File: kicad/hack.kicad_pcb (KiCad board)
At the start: 2 copper layers, 29.2 x 21.6 mm, 35 parts, among them P1 USB_micro, P2 CONN_01X11, P3 CONN_01X11, P4 CONN_01X06, P5 CONN_01X01, U1 MIC5528, U2 STF202, U3 ATSAMD21E, X1 ABS07

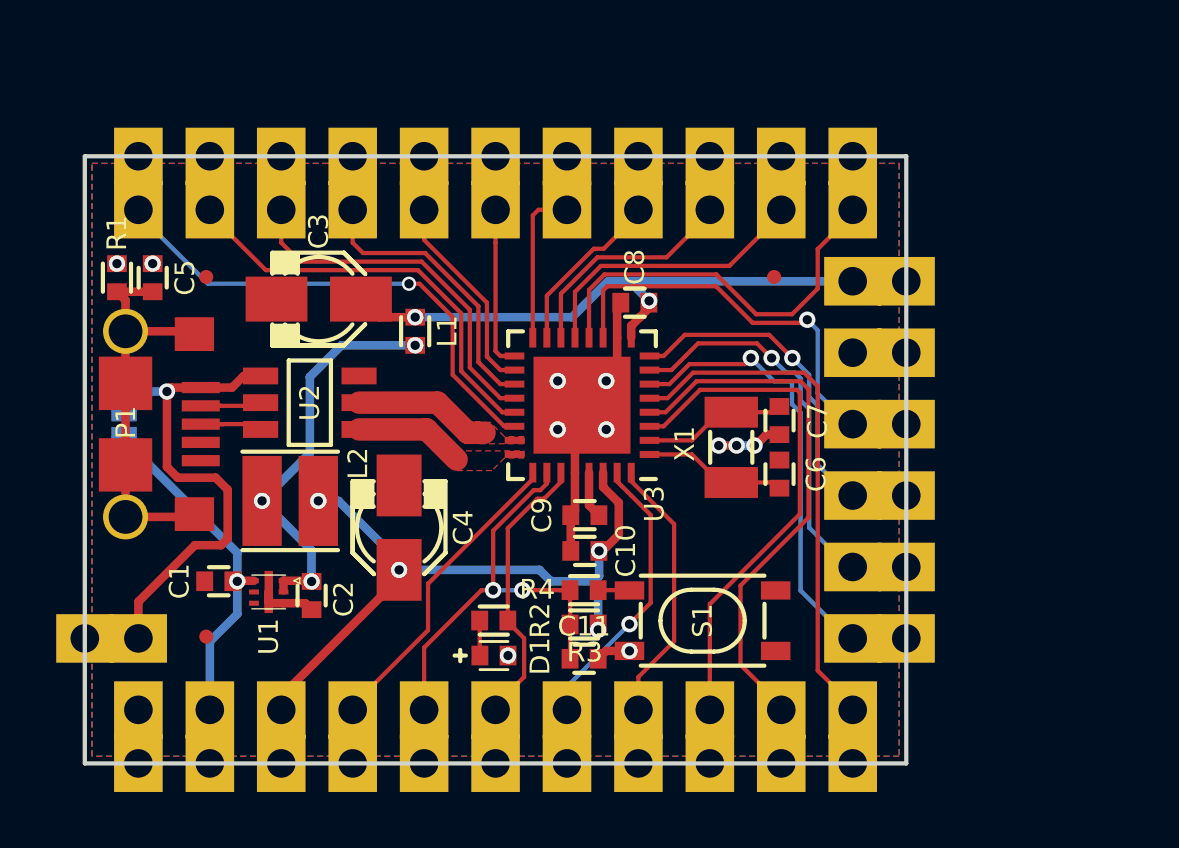
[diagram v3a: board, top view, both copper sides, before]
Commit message: Fixed footprints refereneces on top silkscreen
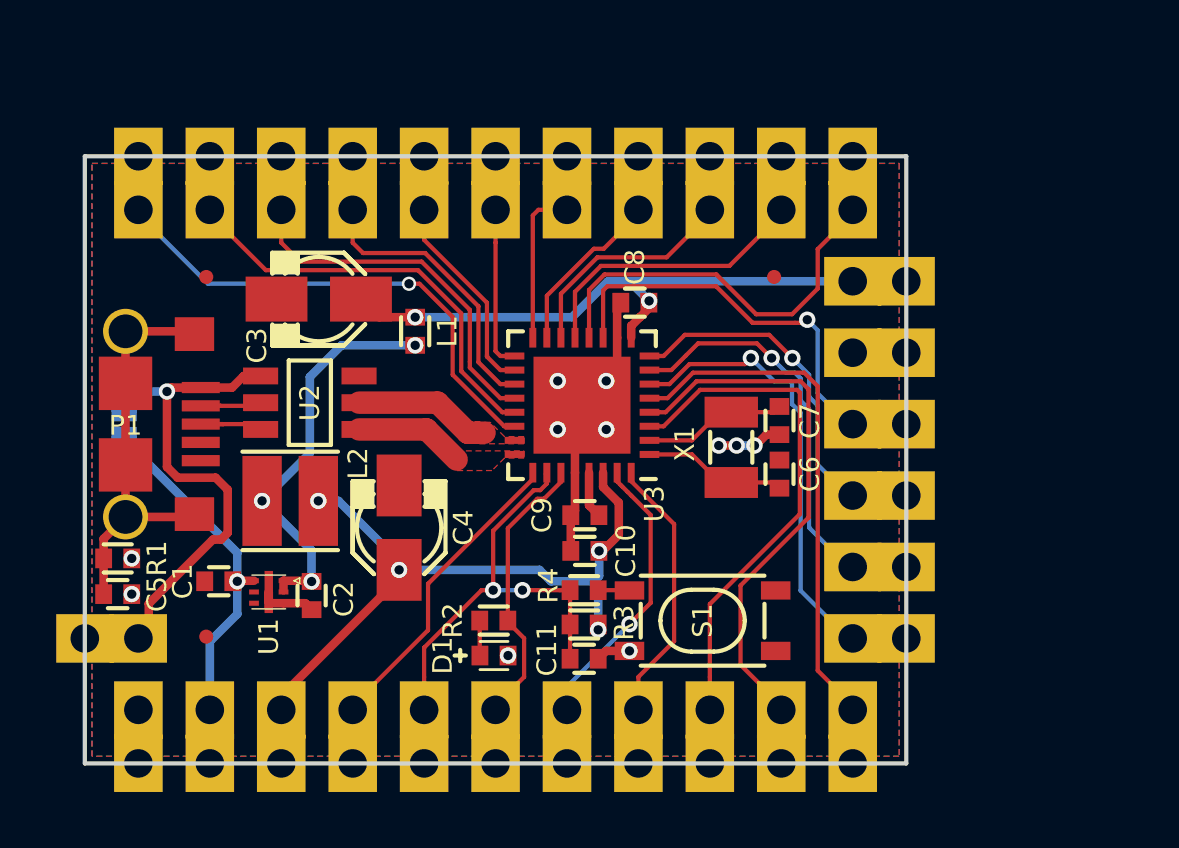
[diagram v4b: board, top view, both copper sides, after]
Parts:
- moved C5 11.3 mm to (154.2, 92.4), turned to 180 degrees
- moved R1 9.98 mm to (154.2, 91.1), turned to 180 degrees
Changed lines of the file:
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@@
     (thickness 1.6)
     (drawings 51)
-    (tracks 388)
+    (tracks 389)
     (zones 0)
     (modules 35)
@@
   (module 10118193-0001LF (layer F.Cu)
     (at 154.4828 86.36)
-    (fp_text reference P1 (at 0.0127 -0.0635 90) (layer F.SilkS)
+    (fp_text reference P1 (at 0 0.0508 180) (layer F.SilkS)
       (effects (font (size 0.7 0.7) (thickness 0.15)))
     )
@@
     (clearance 0.0762)
     (attr smd)
-    (fp_text reference C3 (at 2.413 0 270) (layer F.SilkS)
+    (fp_text reference C3 (at -1.651 -2.1971 270) (layer F.SilkS)
       (effects (font (size 0.7 0.7) (thickness 0.15)))
     )
@@
     (clearance 0.0762)
     (attr smd)
-    (fp_text reference R4 (at -1.6637 -0.0254) (layer F.SilkS)
+    (fp_text reference R4 (at -1.27 -0.1651 90) (layer F.SilkS)
       (effects (font (size 0.7 0.7) (thickness 0.15)))
     )
@@
     (clearance 0.0762)
     (attr smd)
-    (fp_text reference R3 (at 0.0254 0.9906) (layer F.SilkS)
+    (fp_text reference R3 (at 1.4224 -0.0635 90) (layer F.SilkS)
       (effects (font (size 0.7 0.7) (thickness 0.15)))
     )
@@
     (clearance 0.0762)
     (attr smd)
-    (fp_text reference R2 (at -1.651 0 270) (layer F.SilkS)
+    (fp_text reference R2 (at 1.4605 0 270) (layer F.SilkS)
       (effects (font (size 0.7 0.7) (thickness 0.15)))
     )
@@
   )
   (module hack-footprints:R_0603 (layer F.Cu)
-    (at 154.178 81.153 270)
+    (at 154.2034 91.1352 180)
     (descr "Resistor SMD 0603, hand soldering")
     (tags "resistor 0603")
@@
     (clearance 0.0762)
     (attr smd)
-    (fp_text reference R1 (at -1.5875 0 270) (layer F.SilkS)
+    (fp_text reference R1 (at -1.397 0 270) (layer F.SilkS)
       (effects (font (size 0.7 0.7) (thickness 0.15)))
     )
-    (fp_text value 1M (at 0 1.9 270) (layer F.Fab)
+    (fp_text value 1M (at 0 1.9 180) (layer F.Fab)
       (effects (font (size 0.7 0.7) (thickness 0.1)))
     )
@@
     (fp_line (start 0.5 0.5) (end -0.5 0.5) (layer F.SilkS) (width 0.15))
     (fp_line (start -0.5 -0.5) (end 0.5 -0.5) (layer F.SilkS) (width 0.15))
-    (pad 1 smd rect (at -0.5 0 270) (size 0.6 0.7) (layers F.Cu F.Paste F.Mask)
+    (pad 1 smd rect (at -0.5 0 180) (size 0.6 0.7) (layers F.Cu F.Paste F.Mask)
       (net 1 GND) (solder_mask_margin 0.0762) (solder_paste_margin -0.0762) (clearance 0.0762))
-    (pad 2 smd rect (at 0.5 0 270) (size 0.6 0.7) (layers F.Cu F.Paste F.Mask)
+    (pad 2 smd rect (at 0.5 0 180) (size 0.6 0.7) (layers F.Cu F.Paste F.Mask)
       (net 38 /shield) (solder_mask_margin 0.0762) (solder_paste_margin -0.0762) (clearance 0.0762))
     (model RES_SMD_0603.wrl
@@
     (clearance 0.0762)
     (attr smd)
-    (fp_text reference C1 (at 1.397 0 450) (layer F.SilkS)
+    (fp_text reference C1 (at 1.2827 0 450) (layer F.SilkS)
       (effects (font (size 0.7 0.7) (thickness 0.15)))
     )
@@
     (clearance 0.0762)
     (attr smd)
-    (fp_text reference C11 (at 0 -1.15) (layer F.SilkS)
+    (fp_text reference C11 (at -1.3208 -0.3175 90) (layer F.SilkS)
       (effects (font (size 0.7 0.7) (thickness 0.15)))
     )
@@
     (clearance 0.0762)
     (attr smd)
-    (fp_text reference C7 (at 0.0127 -1.3589 270) (layer F.SilkS)
+    (fp_text reference C7 (at 0.0127 -1.0795 270) (layer F.SilkS)
       (effects (font (size 0.7 0.7) (thickness 0.15)))
     )
@@
     (clearance 0.0762)
     (attr smd)
-    (fp_text reference C6 (at 0 1.3081 90) (layer F.SilkS)
+    (fp_text reference C6 (at 0 1.0795 90) (layer F.SilkS)
       (effects (font (size 0.7 0.7) (thickness 0.15)))
     )
@@
   )
   (module hack-footprints:C_0603 (layer F.Cu)
-    (at 155.448 81.153 270)
+    (at 154.2034 92.4052 180)
     (descr "Capacitor SMD 0603, hand soldering")
     (tags "capacitor 0603")
@@
     (clearance 0.0762)
     (attr smd)
-    (fp_text reference C5 (at 0 -1.15 270) (layer F.SilkS)
+    (fp_text reference C5 (at -1.397 0 270) (layer F.SilkS)
       (effects (font (size 0.7 0.7) (thickness 0.15)))
     )
-    (fp_text value 4.7nF (at 0 1.9 270) (layer F.Fab)
+    (fp_text value 4.7nF (at 0 1.9 180) (layer F.Fab)
       (effects (font (size 1 1) (thickness 0.15)))
     )
@@
     (fp_line (start -0.35 -0.5) (end 0.35 -0.5) (layer F.SilkS) (width 0.15))
     (fp_line (start 0.35 0.5) (end -0.35 0.5) (layer F.SilkS) (width 0.15))
-    (pad 1 smd rect (at -0.5 0 270) (size 0.6 0.7) (layers F.Cu F.Paste F.Mask)
+    (pad 1 smd rect (at -0.5 0 180) (size 0.6 0.7) (layers F.Cu F.Paste F.Mask)
       (net 1 GND))
-    (pad 2 smd rect (at 0.5 0 270) (size 0.6 0.7) (layers F.Cu F.Paste F.Mask)
+    (pad 2 smd rect (at 0.5 0 180) (size 0.6 0.7) (layers F.Cu F.Paste F.Mask)
       (net 38 /shield))
     (model Cap_SMD_0603.wrl
@@
     (clearance 0.0762)
     (attr smd)
-    (fp_text reference D1 (at 1.643 0.0254 90) (layer F.SilkS)
+    (fp_text reference D1 (at -1.8241 0 90) (layer F.SilkS)
       (effects (font (size 0.7 0.7) (thickness 0.15)))
     )
@@
     (effects (font (size 0.8 0.8) (thickness 0.2)) (justify right mirror))
   )
-  (gr_text 11 (at 154.94 80.01 270) (layer B.SilkS)
+  (gr_text 11 (at 155.3464 91.8972 180) (layer B.SilkS)
     (effects (font (size 0.8 0.8) (thickness 0.2)) (justify right mirror))
   )
-  (gr_text A4 (at 179.07 91.44 360) (layer B.SilkS)
+  (gr_text A4 (at 179.07 91.44) (layer B.SilkS)
     (effects (font (size 0.8 0.8) (thickness 0.2)) (justify left mirror))
   )
-  (gr_text A3 (at 179.07 93.345 360) (layer B.SilkS)
+  (gr_text A3 (at 179.07 93.345) (layer B.SilkS)
     (effects (font (size 0.8 0.8) (thickness 0.2)) (justify left mirror))
   )
@@
   (gr_line (start 153.416 96.52) (end 153.416 74.93) (layer Margin) (width 0.2))
   (via (at 168.0845 94.5896) (size 0.5842) (drill 0.3302) (layers F.Cu B.Cu) (net 1))
-  (via (at 155.448 80.653) (size 0.5842) (drill 0.3302) (layers F.Cu B.Cu) (net 1))
-  (via (at 154.178 80.653) (size 0.5842) (drill 0.3302) (layers F.Cu B.Cu) (net 1))
+  (via (at 154.7034 92.4052) (size 0.5842) (drill 0.3302) (layers F.Cu B.Cu) (net 1))
+  (via (at 154.7034 91.1352) (size 0.5842) (drill 0.3302) (layers F.Cu B.Cu) (net 1))
   (segment (start 180.34 83.82) (end 182.245 83.82) (width 0.3048) (layer B.Cu) (net 1))
   (via (at 172.4025 94.4245) (size 0.5842) (drill 0.3302) (layers F.Cu B.Cu) (net 1))
@@
   (via (at 159.3375 89.0905) (size 0.5842) (drill 0.3302) (layers F.Cu B.Cu) (net 12))
   (segment (start 160.1005 91.929) (end 160.1005 92.27179) (width 0.3048) (layer F.Cu) (net 12) (status 30))
-  (segment (start 158.115 90.426442) (end 158.115 88.693558) (width 0.3048) (layer F.Cu) (net 13))
+  (segment (start 158.115 88.693558) (end 158.115 90.226442) (width 0.3048) (layer F.Cu) (net 13))
+  (segment (start 158.115 90.226442) (end 157.876641 90.464801) (width 0.3048) (layer F.Cu) (net 13))
+  (segment (start 157.876641 90.464801) (end 157.591599 90.464801) (width 0.3048) (layer F.Cu) (net 13))
+  (segment (start 157.591599 90.464801) (end 155.308201 92.748199) (width 0.3048) (layer F.Cu) (net 13))
+  (segment (start 155.308201 92.748199) (end 155.308201 93.611799) (width 0.3048) (layer F.Cu) (net 13))
+  (segment (start 155.308201 93.611799) (end 154.94 93.98) (width 0.3048) (layer F.Cu) (net 13))
   (segment (start 158.115 88.693558) (end 157.686442 88.265) (width 0.3048) (layer F.Cu) (net 13))
   (segment (start 157.686442 88.265) (end 156.339158 88.265) (width 0.3048) (layer F.Cu) (net 13))
-  (segment (start 156.950399 90.664801) (end 157.876641 90.664801) (width 0.3048) (layer F.Cu) (net 13))
-  (segment (start 157.876641 90.664801) (end 158.115 90.426442) (width 0.3048) (layer F.Cu) (net 13))
-  (segment (start 154.94 93.98) (end 154.94 92.6752) (width 0.3048) (layer F.Cu) (net 13))
-  (segment (start 154.94 92.6752) (end 156.950399 90.664801) (width 0.3048) (layer F.Cu) (net 13))
   (segment (start 154.94 93.98) (end 153.035 93.98) (width 0.3048) (layer B.Cu) (net 13))
   (segment (start 155.956 85.2012) (end 155.956 87.881842) (width 0.3048) (layer F.Cu) (net 13))
@@
   (segment (start 162.56 96.52) (end 162.56 98.425) (width 0.1524) (layer B.Cu) (net 37))
   (segment (start 162.56 96.52) (end 162.56 96.3676) (width 0.1524) (layer B.Cu) (net 37))
+  (segment (start 153.7034 91.1352) (end 153.7034 90.4394) (width 0.3048) (layer F.Cu) (net 38))
+  (segment (start 153.7034 90.4394) (end 154.4828 89.66) (width 0.3048) (layer F.Cu) (net 38))
   (segment (start 154.4828 89.66) (end 156.8328 89.66) (width 0.3048) (layer F.Cu) (net 38))
   (segment (start 156.8328 89.66) (end 156.9328 89.56) (width 0.3048) (layer F.Cu) (net 38))
   (segment (start 154.4828 83.06) (end 156.8328 83.06) (width 0.3048) (layer F.Cu) (net 38))
   (segment (start 156.8328 83.06) (end 156.9328 83.16) (width 0.3048) (layer F.Cu) (net 38))
-  (segment (start 154.178 81.653) (end 155.448 81.653) (width 0.3048) (layer F.Cu) (net 38))
-  (segment (start 154.4828 83.06) (end 154.4828 81.9578) (width 0.3048) (layer F.Cu) (net 38))
-  (segment (start 154.4828 81.9578) (end 154.178 81.653) (width 0.3048) (layer F.Cu) (net 38))
+  (segment (start 153.7034 91.1352) (end 153.7034 92.4052) (width 0.3048) (layer F.Cu) (net 38))
   (segment (start 154.4828 84.91) (end 154.4828 83.06) (width 0.3048) (layer F.Cu) (net 38))
   (segment (start 154.4828 87.81) (end 154.4828 84.91) (width 0.3048) (layer F.Cu) (net 38))

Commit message: Form factor is PDIP-24 now, ready to fab
HACK now fits a PDIP-24 package (its solderable thru-hole headers
spacing is now 0.6"); being longer there's some space on the top side,
so it now features a convenient Cortex SWD Connector, a 2x5 male pin
header with 50 mils spacing in SMD package.
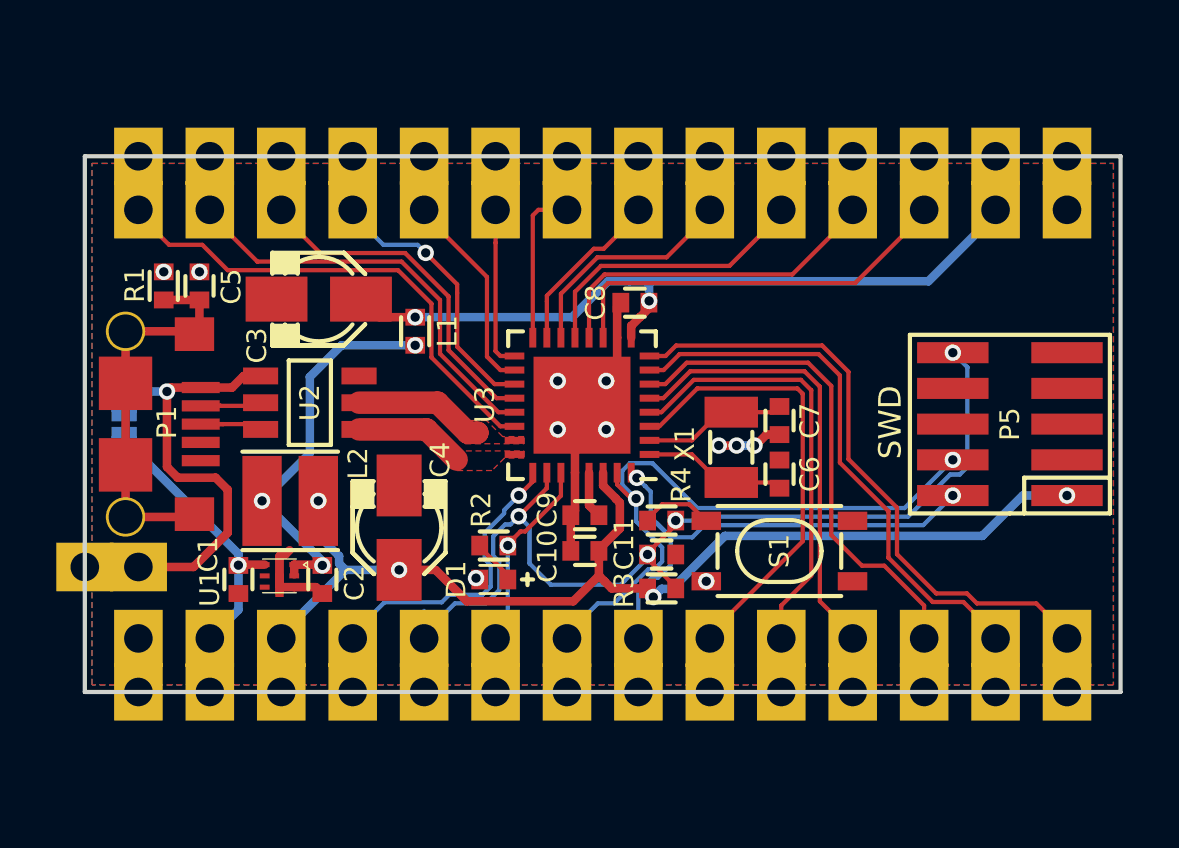
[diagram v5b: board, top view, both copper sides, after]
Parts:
- removed FID1, FID2, FID3: FIDUCIAL, hack-footprints:FIDUCIAL
- P2, P3: value CONN_01X11 -> CONN_01X14; footprint hack-footprints:Pin_Castellated_1x11 -> hack-footprints:Pin_Castellated_1x14
- P4: value CONN_01X06 -> CONN_01X01; footprint hack-footprints:Pin_Castellated_1x06 -> Pin_Castellated_1x01
- P5: value CONN_01X01 -> CONN_SWD; footprint hack-footprints:Pin_Castellated_1x01 -> hack-footprints:Cortex_Debug_Connector_50mils
- U1: footprint hack-footprints:DFN-6-1EP_1.2x1.2mm_Pitch0.4mm -> DFN-6-1EP_1.2x1.2mm_Pitch0.4mm
- moved P5 31.4 mm to (185.9, 88.9)
- moved P4 27.4 mm to (154.9, 91.4), turned to 180 degrees
- moved C5 11.3 mm to (157.1, 81.4), turned to 270 degrees
- moved R1 9.83 mm to (155.8, 81.4), turned to 270 degrees
- moved LOGO1 9.37 mm to (183.6, 85.7)
- moved LOGO3 4.62 mm to (171.4, 84.5)
- moved C11 4.62 mm to (173.5, 91.0)
- moved R4 3.71 mm to (173.5, 89.8), turned to 180 degrees
- moved S1 3.69 mm to (177.7, 90.9)
- moved LOGO2 3.17 mm to (159.4, 85.1)
- moved R3 3.04 mm to (173.5, 92.2), turned to 180 degrees
- moved D1 2.71 mm to (167.6, 91.9), turned to 180 degrees
- moved R2 2.67 mm to (167.6, 90.7)
- moved P2 2.54 mm to (154.9, 94.0)
- moved C1 0.70 mm to (158.5, 91.9), turned to 270 degrees
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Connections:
- P4 pad 1: VDDANA -> VBUS
- P5 pad 1: VBUS -> VDDF
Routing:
- net !RESET: track 17.8 -> 37.3 mm, vias 2 -> 4
- net VDDF: track 26.8 -> 40.7 mm
- net PA30/SWCLK: track 12.1 -> 24.9 mm, vias 1 -> 2
- net PA07/A5: track 13.5 -> 24.1 mm, vias 1 -> 0
- net PA31/SWDIO: track 12.1 -> 20.4 mm, vias 0 -> 2
- net VDDANA: track 22.7 -> 28.6 mm
- net PA06/A4: track 15.7 -> 21.5 mm, vias 1 -> 0
- net PA03/A1: track 21.5 -> 17.6 mm
- net PA28/13: track 12.1 -> 8.86 mm, vias 0 -> 1
- net PA04/A2: track 20.8 -> 18.0 mm
- net PA02/A0: track 20.6 -> 18.1 mm
- net VLDO: track 14.7 -> 12.3 mm
- net PA05/A3: track 17.8 -> 19.8 mm, vias 1 -> 0
- net PA09/1: track 16.2 -> 14.2 mm
- net Net-(R4-Pad2): track 1.12 -> 2.73 mm
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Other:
- board size 29.2 x 21.6 mm -> 36.8 x 19.1 mm
- board text added: "SWD"
